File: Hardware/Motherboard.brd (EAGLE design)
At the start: 124.5 x 73.7 mm, 84 parts, among them J1 MICROMOD-2222-C, J10 MICRO-SD-PUSH-PUSH-EXT-PIN, J2 Vertical Qwiic Connector, J4 QWIIC_RIGHT_ANGLE, J5 CORTEX_JTAG_DEBUG_MINIMUM_PTH, J6 MICROMOD_CARRIER, J7 MICROMOD_CARRIER, U2 MCP73831, U5 AP7361C-33

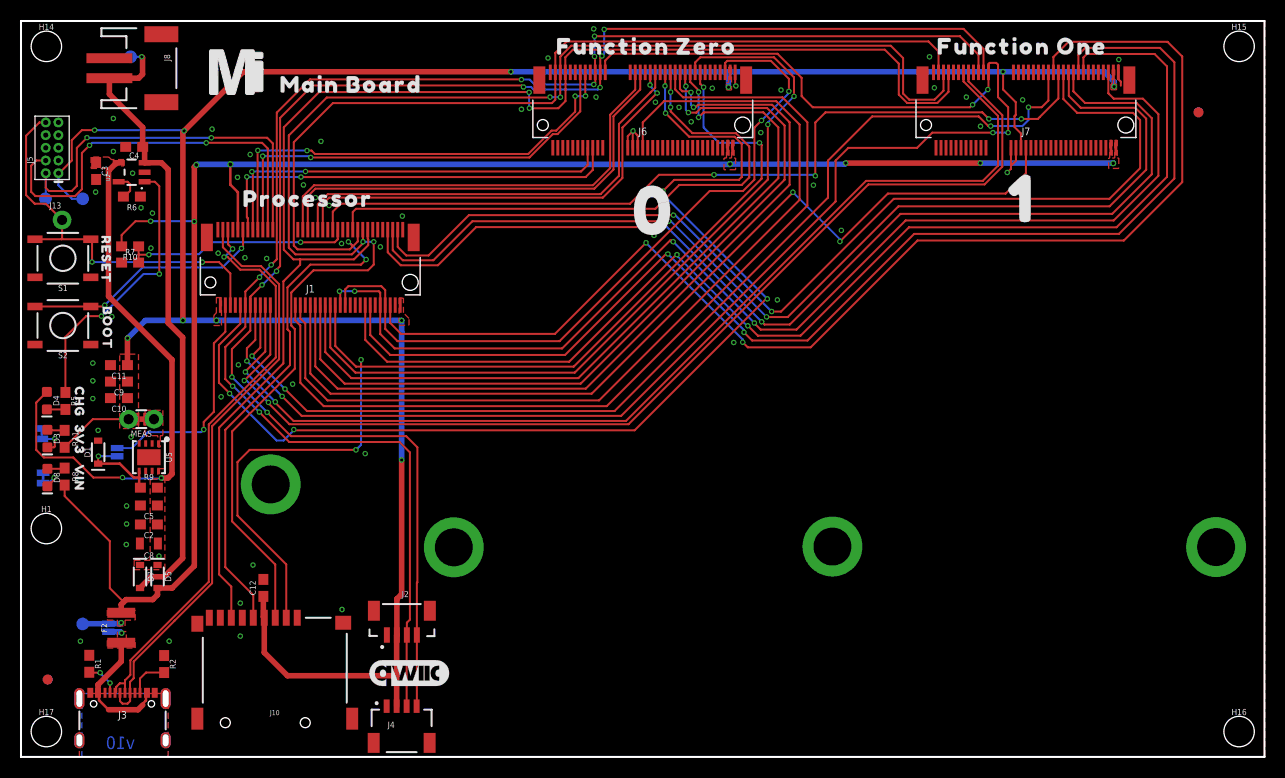
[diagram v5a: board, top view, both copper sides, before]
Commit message: Adds 2 pin dip switch for charge selection, switches diode to PCHN MOSFET to VBAT net
* Adds better silk
*  Adds charge selection table to schematic
* Moves standoffs around
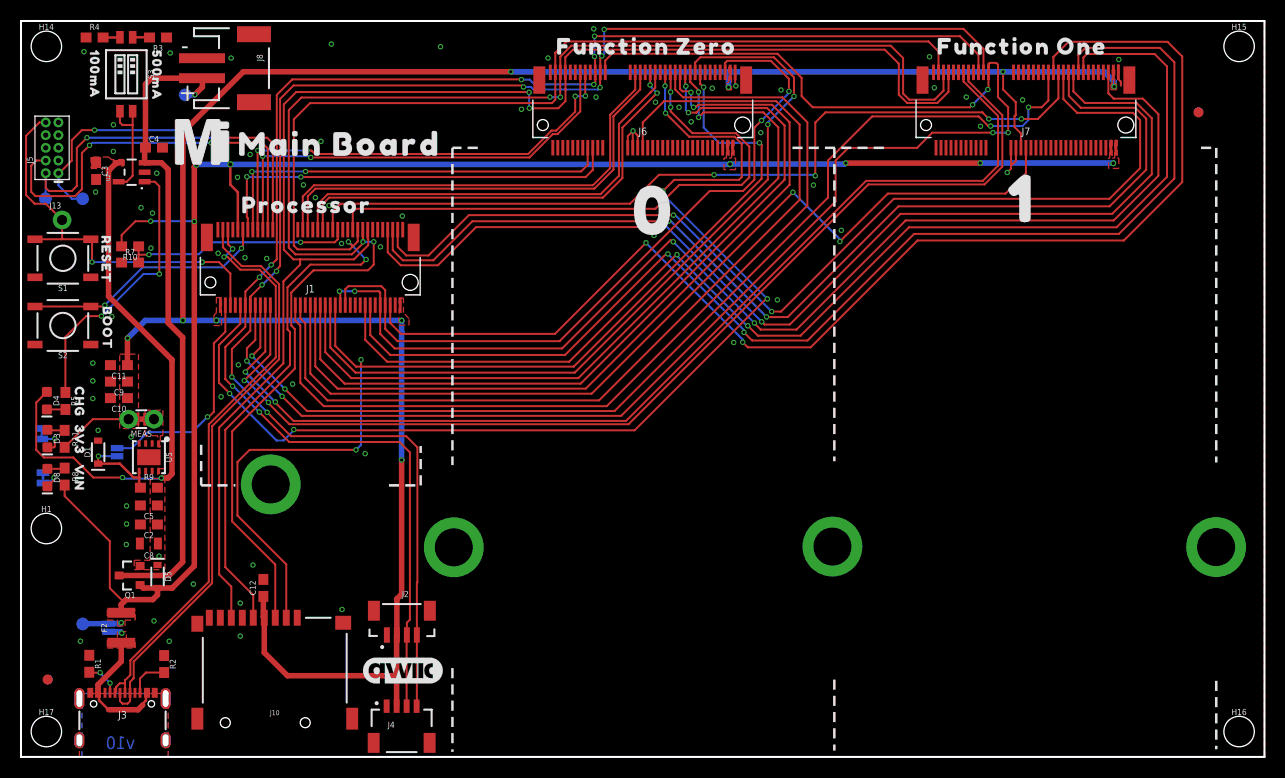
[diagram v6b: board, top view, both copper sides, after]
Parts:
- removed D7: 3A/10V/280mV, SparkFun-DiscreteSemi:SOD-323
- removed R6: 2.0k, SparkFun-Resistors:0603
- added Q1: 20V/4.2A/52mΩ/1.4W, SparkFun-DiscreteSemi:SOT23-3
- added R3: 2.0k, SparkFun-Resistors:0603
- added R4: 10k, SparkFun-Resistors:0603
- added S3: DIP-02-SMD-50MIL, SparkFun-Switches:DIPSWITCH-02-50MIL
- added U$19: (no value), top:100MA6
- added U$20: (no value), top:500MA101
- added U$21: (no value), top:MAIN_BOARD5523
- LOGO3: value OSHW-LOGOS -> OSHW-LOGOL; device SparkFun-Aesthetics:OSHW-LOGO-S -> SparkFun-Aesthetics:OSHW-LOGO-L
- U$17: device top:MAIN_BOARD522 -> SparkFun-MicroMod:MICROMOD_LOGO_1
- moved U$17 50.4 mm to (61.0, 25.4), flipped to the bottom
- moved J8 9.27 mm to (21.8, 68.9)
- moved U$14 7.78 mm to (18.2, 61.6)
- moved U$13 7.62 mm to (67.3, 19.1)
- moved U$18 7.62 mm to (55.9, 19.1)
- moved TP3 6.66 mm to (16.4, 66.3)
- moved C4 1.98 mm to (13.3, 61.0), turned to 0 degrees
- moved LOGO3 1.44 mm to (119.6, 8.64)
- moved LOGO1 0.68 mm to (38.2, 8.64)
- moved U$10 0.65 mm to (28.6, 55.2)
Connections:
- new net N$6: S3.3, S3.4, U2.5
- new net N$9: R4.2, S3.2
- net GND: now also R3.1, R4.1; no longer R6.1
- net N$8: now also R3.2, S3.1; no longer R6.2, U2.5
- net VCC: now also Q1.2; no longer D7.C
- net VIN: now also Q1.1
- net V_BATT: now also Q1.3; no longer D7.A
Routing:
- net N$6: track 0.00 -> 10.6 mm
- net V_BATT: track 64.0 -> 66.0 mm
- net VIN: track 176.1 -> 178.0 mm
- net N$9: track 0.00 -> 1.70 mm
- net SPI_PROCESSOR_SDO: track 148.8 -> 150.3 mm
- net SPI_PROCESSOR_SDI: track 144.0 -> 145.4 mm
- net SPI_PROCESSOR_SCK: track 141.6 -> 142.9 mm
- net N$8: track 2.83 -> 1.70 mm
- net I2C_SCL: track 156.2 -> 157.3 mm
- net I2C_SDA: track 155.1 -> 156.1 mm
- net GND: vias 64 -> 72
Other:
- board text added: "+"
- board text added: "-"

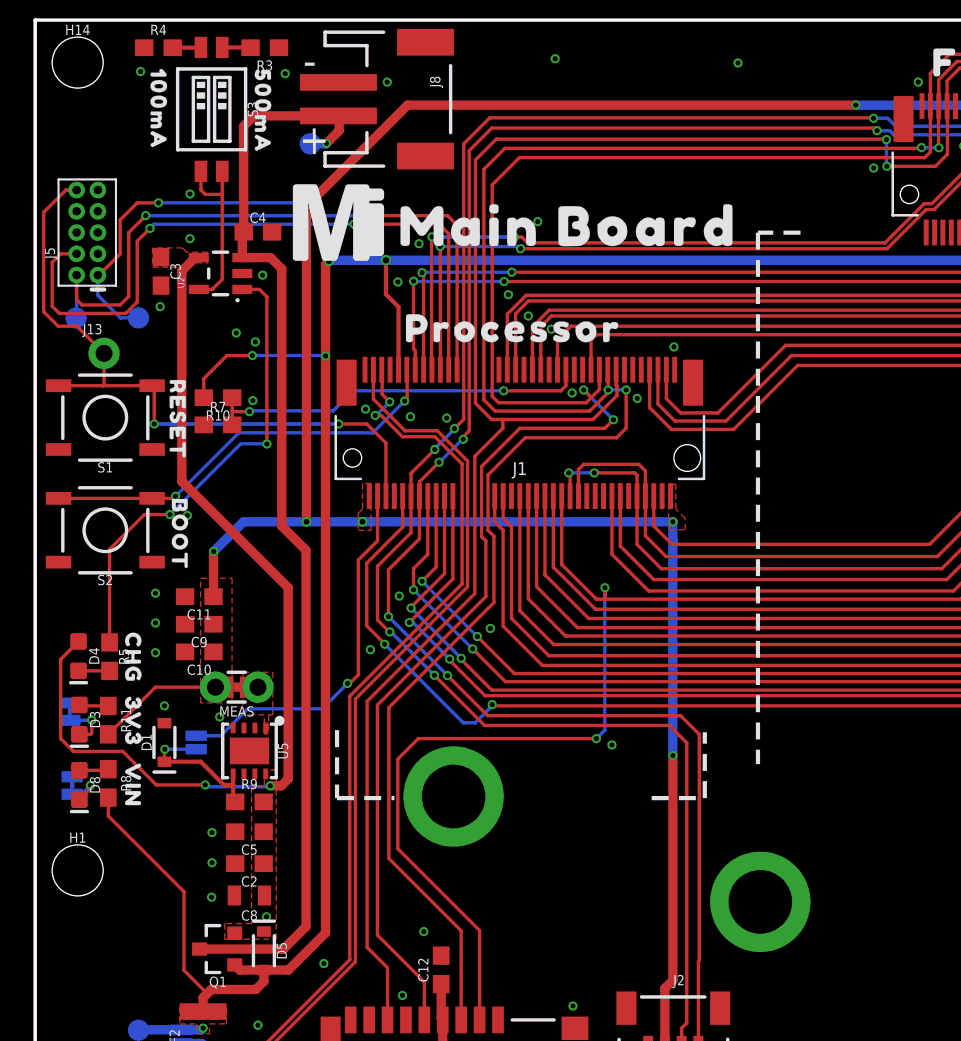
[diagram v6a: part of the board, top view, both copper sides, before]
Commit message: Adds qwiic standoff silk
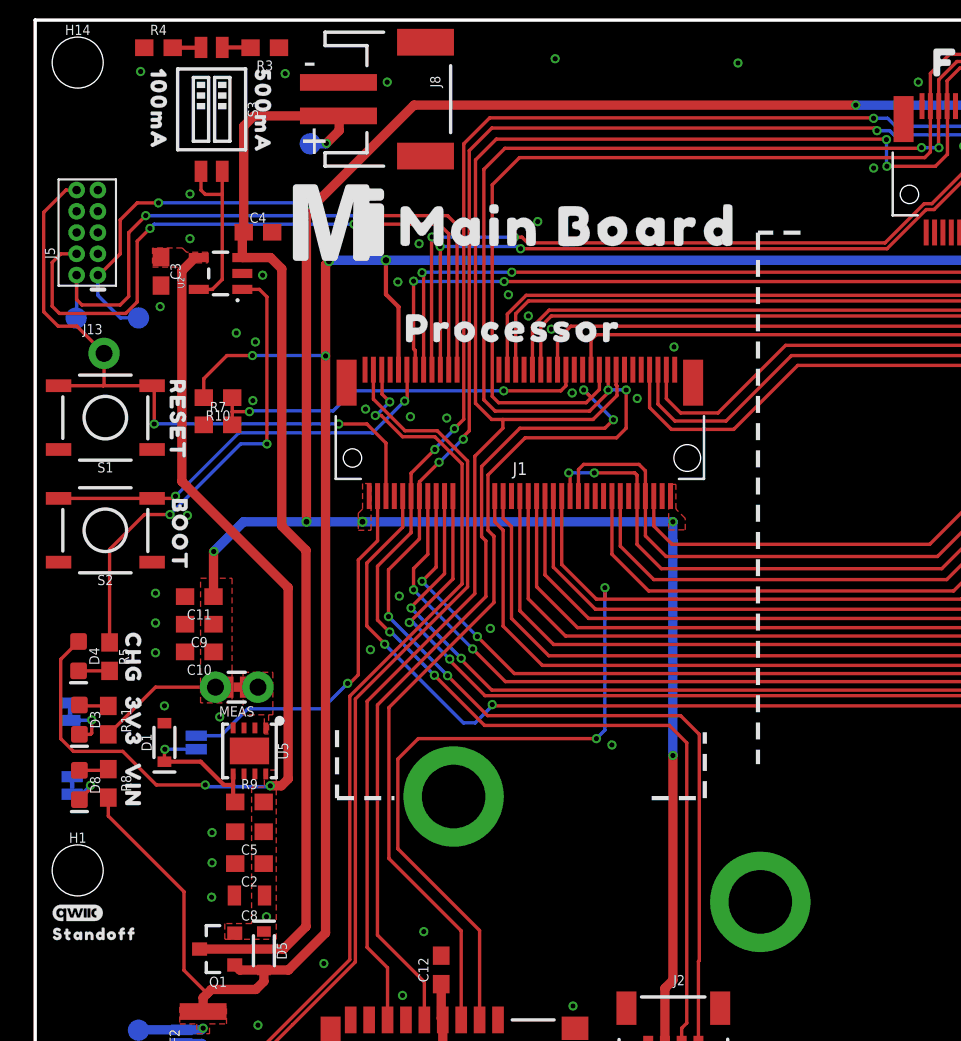
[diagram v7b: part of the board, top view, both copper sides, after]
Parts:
- added U$22: (no value), SparkFun-Aesthetics:QWIIC_3MM
- added U$23: (no value), top:STANDOFF501
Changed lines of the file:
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@@
 <layer number="37" name="tTest" color="7" fill="1" visible="no" active="yes"/>
 <layer number="38" name="bTest" color="7" fill="1" visible="no" active="yes"/>
-<layer number="39" name="tKeepout" color="4" fill="11" visible="yes" active="yes"/>
+<layer number="39" name="tKeepout" color="4" fill="11" visible="no" active="yes"/>
 <layer number="40" name="bKeepout" color="1" fill="11" visible="no" active="yes"/>
 <layer number="41" name="tRestrict" color="4" fill="10" visible="no" active="yes"/>
@@
 <element name="U$21" library="top" package="MAIN_BOARD5523" value="" x="31.877" y="61.341" smashed="yes"/>
 <element name="U$17" library="SparkFun-MicroMod" package="MICROMOD_LOGO_1" value="" x="60.96" y="25.4" smashed="yes" rot="MR0"/>
+<element name="U$22" library="SparkFun-Aesthetics" package="QWIIC_3MM" value="" x="2.54" y="20.32" smashed="yes"/>
+<element name="U$23" library="top" package="STANDOFF501" value="" x="3.556" y="19.05" smashed="yes"/>
 </elements>
 <signals>
@@
 <wire x1="38.0996" y1="42.4946" x2="38.1" y2="42.4942" width="0.5588" layer="16"/>
 <wire x1="38.1" y1="42.4942" x2="38.1" y2="43.688" width="0.5588" layer="16"/>
-<wire x1="22.2504" y1="68.58" x2="16.3322" y2="62.6618" width="0.5588" layer="1"/>
+<wire x1="22.6314" y1="68.58" x2="16.7132" y2="62.6618" width="0.5588" layer="1"/>
+<wire x1="16.7132" y1="62.6618" x2="16.3322" y2="62.6618" width="0.5588" layer="1"/>
 <wire x1="16.2052" y1="62.5348" x2="16.3322" y2="62.6618" width="0.5588" layer="1"/>
-<wire x1="22.2504" y1="68.58" x2="49.022" y2="68.58" width="0.5588" layer="1"/>
+<wire x1="22.6314" y1="68.58" x2="49.022" y2="68.58" width="0.5588" layer="1"/>
 <via x="49.022" y="68.58" extent="1-16" drill="0.3048"/>
 <wire x1="49.022" y1="68.58" x2="70.8152" y2="68.58" width="0.5588" layer="16"/>

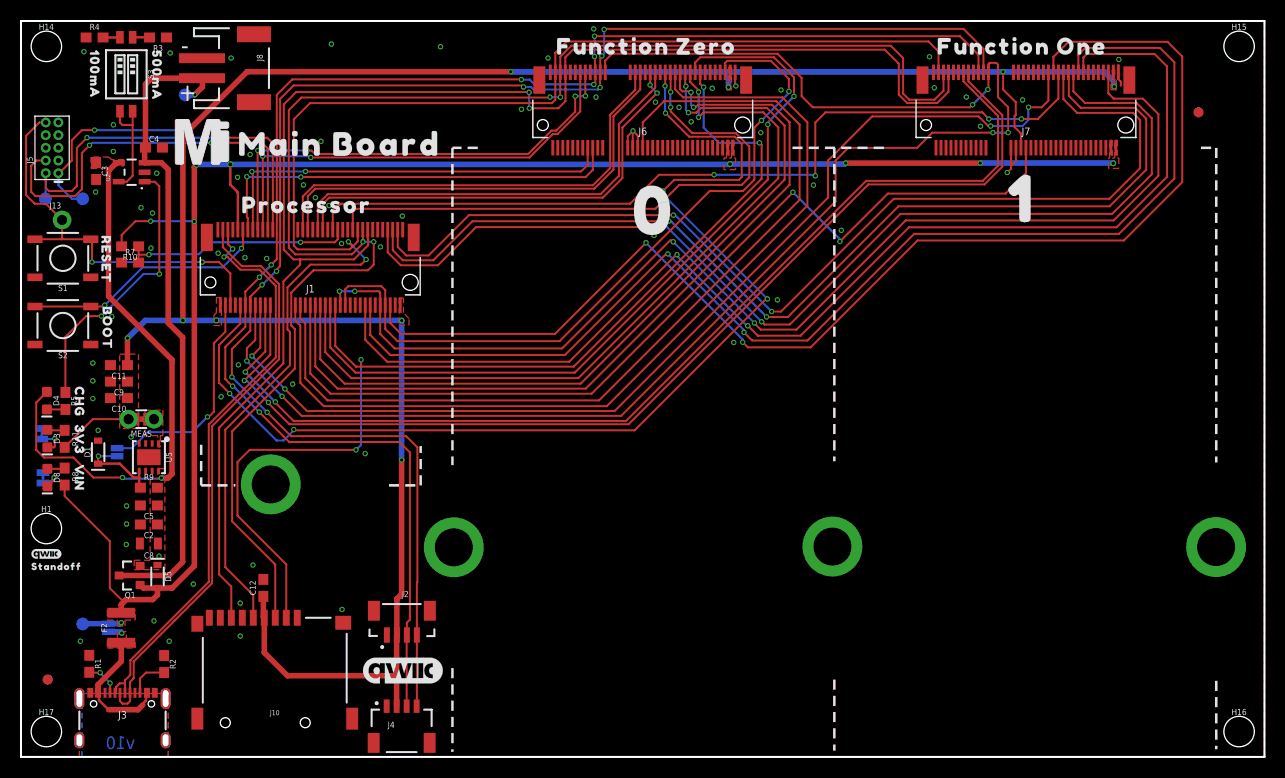
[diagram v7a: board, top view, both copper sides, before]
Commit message: Replace MOSFET with another one
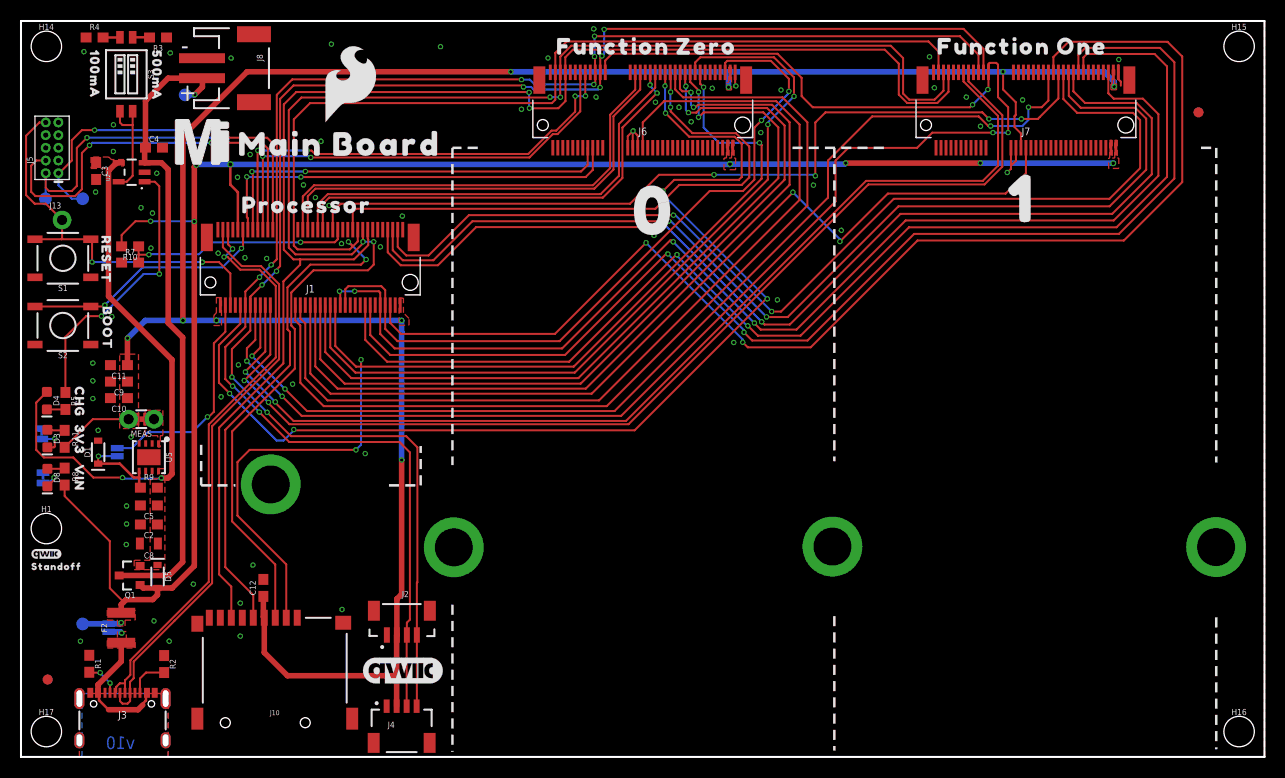
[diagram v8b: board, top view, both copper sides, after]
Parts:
- added U$24: (no value), SparkFun-Aesthetics:SFE_LOGO_FLAME_.3
- Q1: value 20V/4.2A/52mΩ/1.4W -> 3.1A/30V/105mΩ
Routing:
- net V_BATT: track 66.0 -> 65.1 mm
- net VCC: vias 3 -> 2
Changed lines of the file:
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@@
 <wire x1="45.72" y1="60.96" x2="43.18" y2="60.96" width="0.254" layer="21" style="shortdash"/>
 <wire x1="43.18" y1="60.96" x2="43.18" y2="29.21" width="0.254" layer="21" style="shortdash"/>
-<wire x1="81.407" y1="7.747" x2="81.407" y2="0.635" width="0.254" layer="21" style="shortdash"/>
-<wire x1="119.634" y1="7.62" x2="119.634" y2="0.762" width="0.254" layer="21" style="shortdash"/>
-<wire x1="43.18" y1="8.89" x2="43.18" y2="0.508" width="0.254" layer="21" style="shortdash"/>
+<wire x1="81.407" y1="14.097" x2="81.407" y2="0.635" width="0.254" layer="21" style="shortdash"/>
+<wire x1="119.634" y1="13.97" x2="119.634" y2="0.762" width="0.254" layer="21" style="shortdash"/>
+<wire x1="43.18" y1="15.24" x2="43.18" y2="0.508" width="0.254" layer="21" style="shortdash"/>
 <wire x1="18.034" y1="31.242" x2="18.034" y2="27.178" width="0.254" layer="21" style="shortdash"/>
 <wire x1="18.034" y1="27.178" x2="21.463" y2="27.178" width="0.254" layer="21" style="shortdash"/>
@@
 <element name="U$19" library="top" package="100MA6" value="" x="7.366" y="68.326" smashed="yes" rot="R270"/>
 <element name="U$20" library="top" package="500MA101" value="" x="13.589" y="68.199" smashed="yes" rot="R270"/>
-<element name="Q1" library="SparkFun-DiscreteSemi" package="SOT23-3" value="20V/4.2A/52mΩ/1.4W" x="10.922" y="18.161" smashed="yes" rot="R90">
+<element name="Q1" library="SparkFun-DiscreteSemi" package="SOT23-3" value="3.1A/30V/105mΩ" x="10.922" y="18.161" smashed="yes" rot="R90">
 <attribute name="NAME" x="10.922" y="16.51" size="0.6096" layer="25" font="vector" ratio="20" rot="R180" align="bottom-center"/>
-<attribute name="PROD_ID" value="TRANS-14388" x="10.922" y="18.161" size="1.778" layer="27" font="vector" ratio="15" rot="R90" display="off"/>
-<attribute name="VALUE" x="10.922" y="19.812" size="0.6096" layer="27" font="vector" ratio="20" rot="R180" align="top-center"/>
+<attribute name="PROD_ID" value="TRANS-11308" x="10.922" y="18.161" size="1.778" layer="27" font="vector" ratio="15" rot="R90" display="off"/>
+<attribute name="VALUE" value="3.1A/30V/105mΩ" x="10.922" y="19.812" size="0.6096" layer="27" font="vector" ratio="20" rot="R180" align="top-center"/>
 </element>
 <element name="U$21" library="top" package="MAIN_BOARD5523" value="" x="31.877" y="61.341" smashed="yes"/>
@@
 <element name="U$22" library="SparkFun-Aesthetics" package="QWIIC_3MM" value="" x="2.54" y="20.32" smashed="yes"/>
 <element name="U$23" library="top" package="STANDOFF501" value="" x="3.556" y="19.05" smashed="yes"/>
+<element name="U$24" library="SparkFun-Aesthetics" package="SFE_LOGO_FLAME_.3" value="" x="33.02" y="67.31" smashed="yes"/>
 </elements>
 <signals>
@@
 <wire x1="14.732" y1="43.434" x2="14.732" y2="58.801" width="0.5588" layer="1"/>
 <wire x1="12.3745" y1="59.4716" x2="12.3745" y2="60.8655" width="0.5588" layer="1"/>
-<wire x1="13.0716" y1="67.9356" x2="18.1186" y2="67.9356" width="0.5588" layer="1"/>
-<wire x1="12.4596" y1="60.9854" x2="12.4596" y2="67.3236" width="0.5588" layer="1"/>
-<wire x1="12.4596" y1="67.3236" x2="13.0716" y2="67.9356" width="0.5588" layer="1"/>
+<wire x1="14.7226" y1="67.9356" x2="18.1186" y2="67.9356" width="0.5588" layer="1"/>
+<wire x1="12.4596" y1="60.9854" x2="12.4596" y2="65.6726" width="0.5588" layer="1"/>
+<wire x1="12.4596" y1="65.6726" x2="14.7226" y2="67.9356" width="0.5588" layer="1"/>
 <wire x1="16.4338" y1="66.2686" x2="17.3736" y2="66.2686" width="0.5588" layer="16"/>
 <wire x1="17.3736" y1="66.2686" x2="17.399" y2="66.294" width="0.5588" layer="16"/>
@@
 <vertex x="9.0424" y="59.1566"/>
 </polygon>
-<via x="13.8176" y="20.0914" extent="1-16" drill="0.3048"/>
 <wire x1="2.591425" y1="36.5358" x2="1.524" y2="35.468375" width="0.2032" layer="1"/>
 <wire x1="1.524" y1="30.734" x2="2.286" y2="29.972" width="0.2032" layer="1"/>
